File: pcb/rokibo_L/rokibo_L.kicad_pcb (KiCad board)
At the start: 2 copper layers, 52 parts, among them SW000 SW_Push, SW001 SW_Push, SW002 SW_Push, SW003 SW_Push, SW004 SW_Push, SW005 SW_Push, SW006 SW_Push, SW007 SW_Push, SW008 SW_Push, SW009 SW_Push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

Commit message: fix: Draw symmetric edge cut
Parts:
- removed H007: ~, MountingHole:MountingHole_4.3mm_M4
- added H002: ~, rokibo:m2_Spacer_Hole, F.Cu at (124.1, 133.1)
- BT000: footprint roBa:JST_S2B-PH-SM4-TB -> rokibo:JST_S2B-PH-SM4-TB; moved to B.Cu
- D000, D001, D002, D003, D004, D005, D006, D007, D008, D009, D010, D011, D012, D013, D014, D015, D016, D017, D018, D019, D020: footprint kbd_Parts:Diode_SMD -> rokibo:Diode_SMD
- H000, H001, H003, H004, H005, H006: footprint MountingHole:MountingHole_4.3mm_M4 -> rokibo:m2_Spacer_Hole
- SW021: footprint roBa:MSK-12C02 -> rokibo:TGSW_MSK-12D19
- U000: footprint roBa:XIAO_nRF52840_wBAT_wNFC -> rokibo:XIAO_nRF52840_wBAT_wNFC
- moved SW017 341.2 mm to (185.7, 88.4)
- moved SW020 327.3 mm to (214.3, 128.9), turned to -15 degrees
- moved SW005 322.7 mm to (130.4, 83.7)
- moved SW019 319.4 mm to (192.6, 126.2)
- moved SW011 316.3 mm to (148.8, 114.3)
- moved SW018 315.5 mm to (185.7, 105.7)
- moved SW015 311.8 mm to (170.7, 128.9), turned to 15 degrees
- moved SW009 308.6 mm to (148.8, 79.8)
- moved SW010 308.6 mm to (148.8, 97.0)
- moved SW013 303.5 mm to (167.3, 83.6)
- moved SW006 294.4 mm to (130.4, 100.9)
- moved SW014 294.2 mm to (167.3, 100.9)
- moved D020 291.0 mm to (209.2, 125.0)
- moved SW007 290.8 mm to (130.4, 118.2)
- moved SW003 287.9 mm to (111.9, 130.4)
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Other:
- board outline added: 124.6 x 85.4 mm

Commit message: feat: Draw left track
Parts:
- U000: footprint rokibo:XIAO_nRF52840_wBAT_wNFC -> rokibo:XIAO_nRF52840_wBAT_wNFC_1
- moved H004 16.4 mm to (211.6, 89.0)
- moved SW021 1.56 mm to (214.8, 113.6)
- moved H005 0.66 mm to (182.2, 127.7)
- moved BT000 0.63 mm to (203.8, 82.9)
- moved U000 0.60 mm to (205.7, 62.6)
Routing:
- net Col0: track 0.00 -> 220.6 mm, vias 0 -> 1
- net Col1: track 0.00 -> 192.9 mm, vias 0 -> 8
- net Row3: track 0.00 -> 191.0 mm, vias 0 -> 5
- net Col2: track 0.00 -> 186.2 mm, vias 0 -> 8
- net Col3: track 0.00 -> 172.8 mm, vias 0 -> 6
- net Row2: track 0.00 -> 169.7 mm, vias 0 -> 1
- net Row1: track 0.00 -> 151.4 mm, vias 0 -> 1
- net Col4: track 0.00 -> 148.3 mm, vias 0 -> 7
- net Row0: track 0.00 -> 143.4 mm, vias 0 -> 1
- net Col5: track 0.00 -> 76.6 mm, vias 0 -> 3
- net GND: track 0.00 -> 64.9 mm
- net Net-(BT000--): track 0.00 -> 43.6 mm
- net Net-(D015-A): track 0.00 -> 29.9 mm
- net Net-(D016-A): track 0.00 -> 24.8 mm
- net Net-(D003-A): track 0.00 -> 23.8 mm
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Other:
- outline, holes or cut-outs redrawn

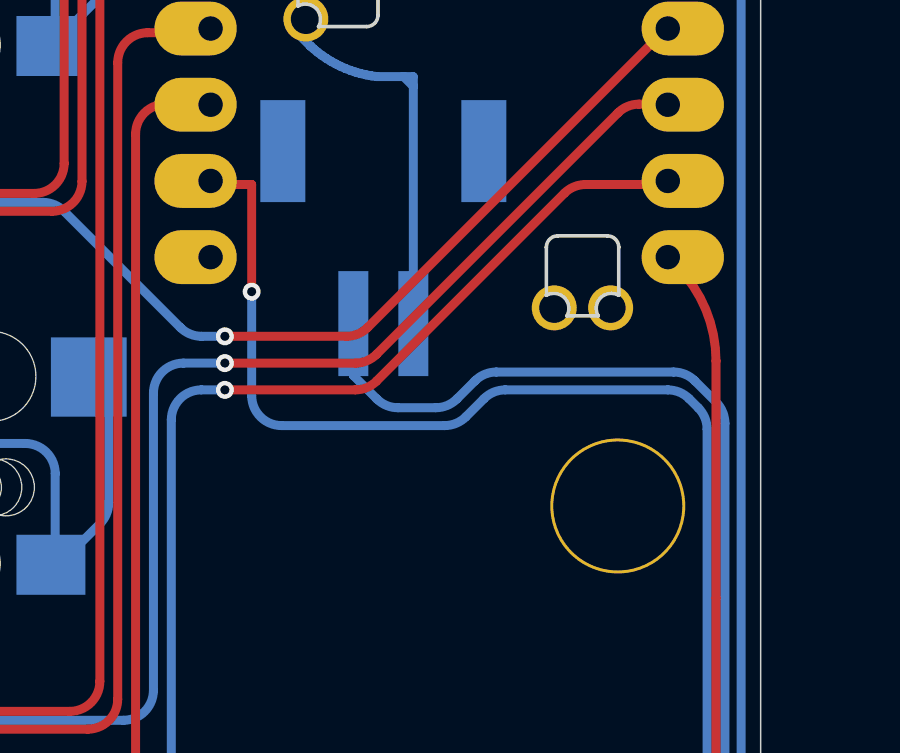
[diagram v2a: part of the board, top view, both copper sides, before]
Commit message: fix: Update tracks
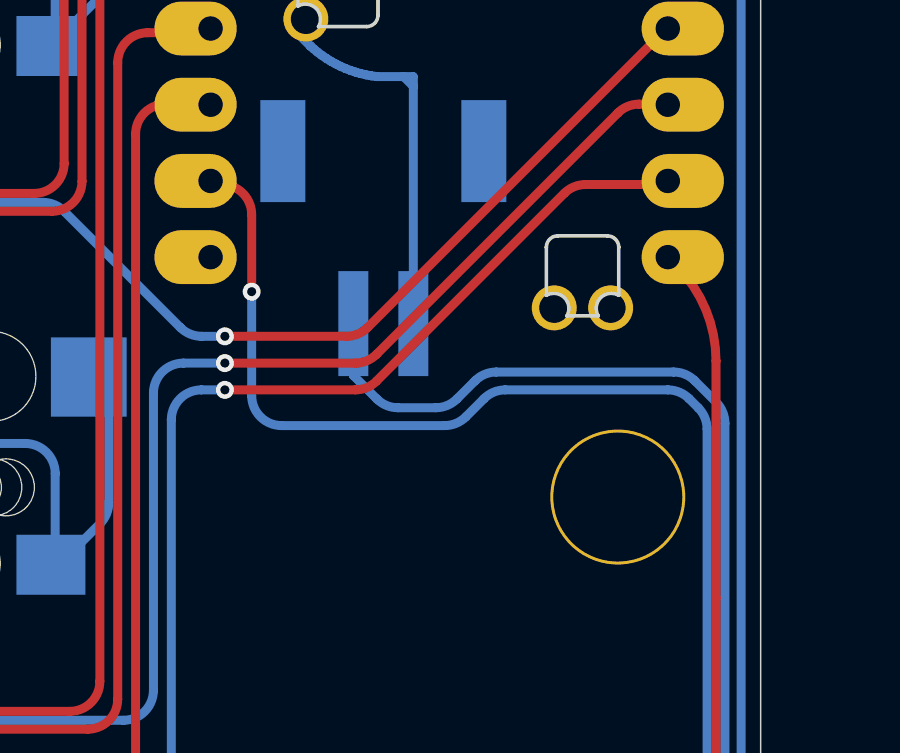
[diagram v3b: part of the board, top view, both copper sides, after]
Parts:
- moved H004 0.30 mm to (211.6, 88.7)
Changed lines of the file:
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@@
 	(footprint "rokibo:m2_Spacer_Hole"
 		(layer "F.Cu")
-		(at 211.633416 88.999144)
+		(at 211.633416 88.701488)
 		(descr "Mounting Hole 2.2mm, no annular, M2")
 		(tags "mounting hole 2.2mm no annular m2")
@@
 	(segment
 		(start 199.42952 81.8554)
-		(end 199.42952 78.283528)
+		(end 199.42952 79.283528)
 		(width 0.3)
 		(layer "F.Cu")
@@
 	)
 	(segment
-		(start 199.42952 78.283528)
+		(start 198.42952 78.283528)
 		(end 198.347723 78.283528)
 		(width 0.3)
@@
 		(width 0.3)
 		(layer "F.Cu")
+		(net 33)
+	)
+	(arc
+		(start 199.42952 79.283528)
+		(mid 199.136627 78.576421)
+		(end 198.42952 78.283528)
+		(width 0.3)
+		(layer "F.Cu")
